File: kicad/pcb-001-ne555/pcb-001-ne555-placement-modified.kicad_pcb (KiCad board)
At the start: 2 copper layers, 14 parts, among them J1 +5 V / GND power input, U1 NE555D

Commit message: Update project files 2026-08-16 01:39:38
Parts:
- moved TP3 33.3 mm to (134.5, 108.0)
- moved RV1 24.8 mm to (107.0, 117.0), turned to -90 degrees
- moved D1 21.8 mm to (130.7, 117.4)
- moved U1 21.6 mm to (127.2, 107.6), turned to 180 degrees
- moved TP4 19.7 mm to (117.0, 110.5)
- moved R2 19.3 mm to (110.5, 100.2), turned to -90 degrees
- moved R1 18.9 mm to (106.5, 90.4), turned to -90 degrees
- moved C1 16.1 mm to (114.2, 104.0)
- moved R3 14.0 mm to (129.9, 101.9)
- moved C2 13.3 mm to (111.8, 95.8)
- moved J1 13.1 mm to (125.2, 88.2)
- moved TP1 4.48 mm to (106.5, 86.0)
- moved TP2 4.00 mm to (110.8, 86.0)
- moved C3 3.54 mm to (121.5, 112.8)
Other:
- board outline added: 39.2 x 41.8 mm

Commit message: Update project files 2026-08-16 14:48:06
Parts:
- U1: value NE555D -> NE555P
- moved TP2 38.6 mm to (139.8, 111.5)
- moved TP1 12.3 mm to (118.8, 85.8)
- moved J1 11.0 mm to (136.0, 86.2), turned to -90 degrees
- moved R1 5.02 mm to (106.0, 85.4)
- moved R2 4.49 mm to (110.5, 95.7)
- moved C2 4.26 mm to (112.0, 91.5)
- moved TP4 2.76 mm to (114.2, 110.2)
- moved RV1 2.37 mm to (109.2, 118.0)
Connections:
- D1 pad 1: /VOUT -> Net-(D1-K)
- R3 pad 1: /VOUT -> Net-(D1-K)
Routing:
- net +5V: track 0.00 -> 69.8 mm
- net /VCAP: track 0.00 -> 33.7 mm
- net Net-(U1-DISCH): track 0.00 -> 28.7 mm
- net /VOUT: track 0.00 -> 19.4 mm
- net Net-(D1-K): track 0.00 -> 15.8 mm
- net Net-(R2-Pad2): track 0.00 -> 12.7 mm
- net Net-(U1-CONT): track 0.00 -> 11.0 mm
- net GND: track 0.00 -> 5.44 mm
- added copper zone on B.Cu, net GND
- added copper zone on F.Cu, net GND
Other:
- board size 39.2 x 41.8 mm -> 38.5 x 40.8 mm

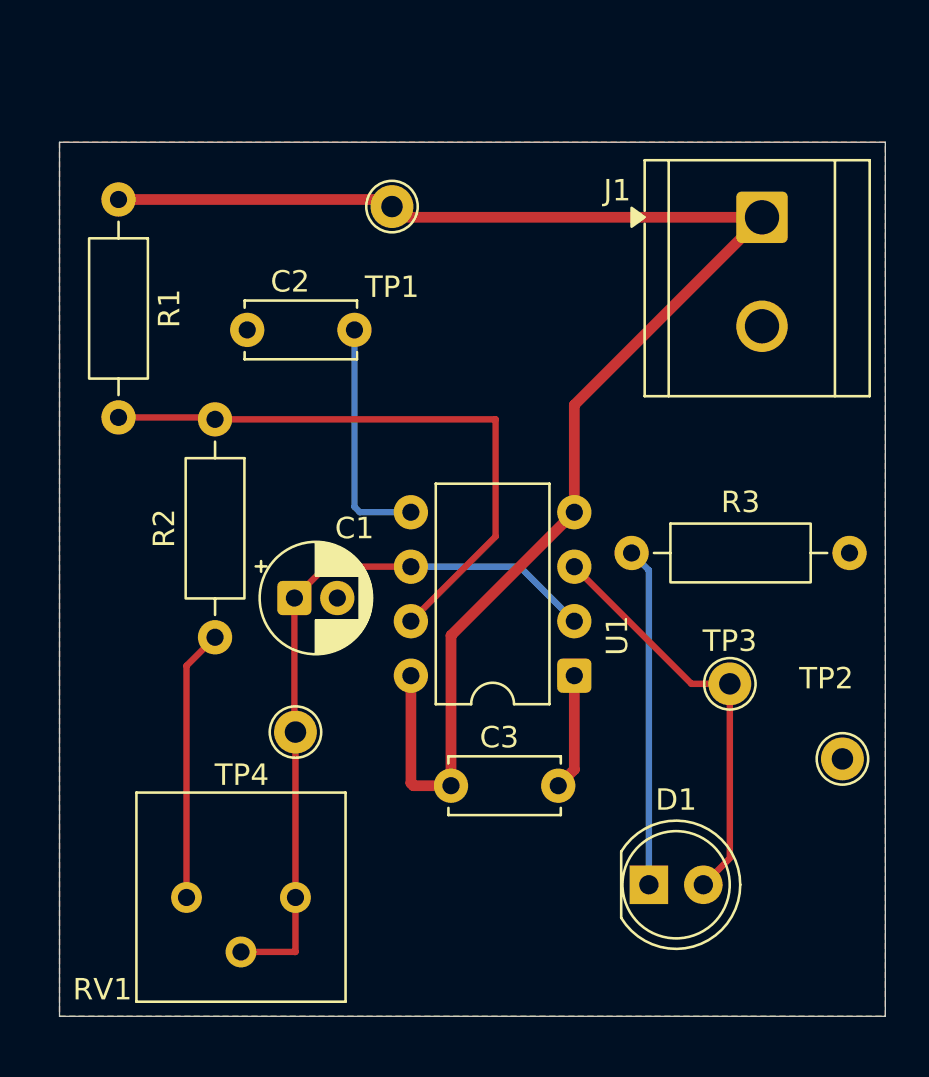
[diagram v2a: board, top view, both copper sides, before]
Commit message: docs: publish final PCB-001 engineering record
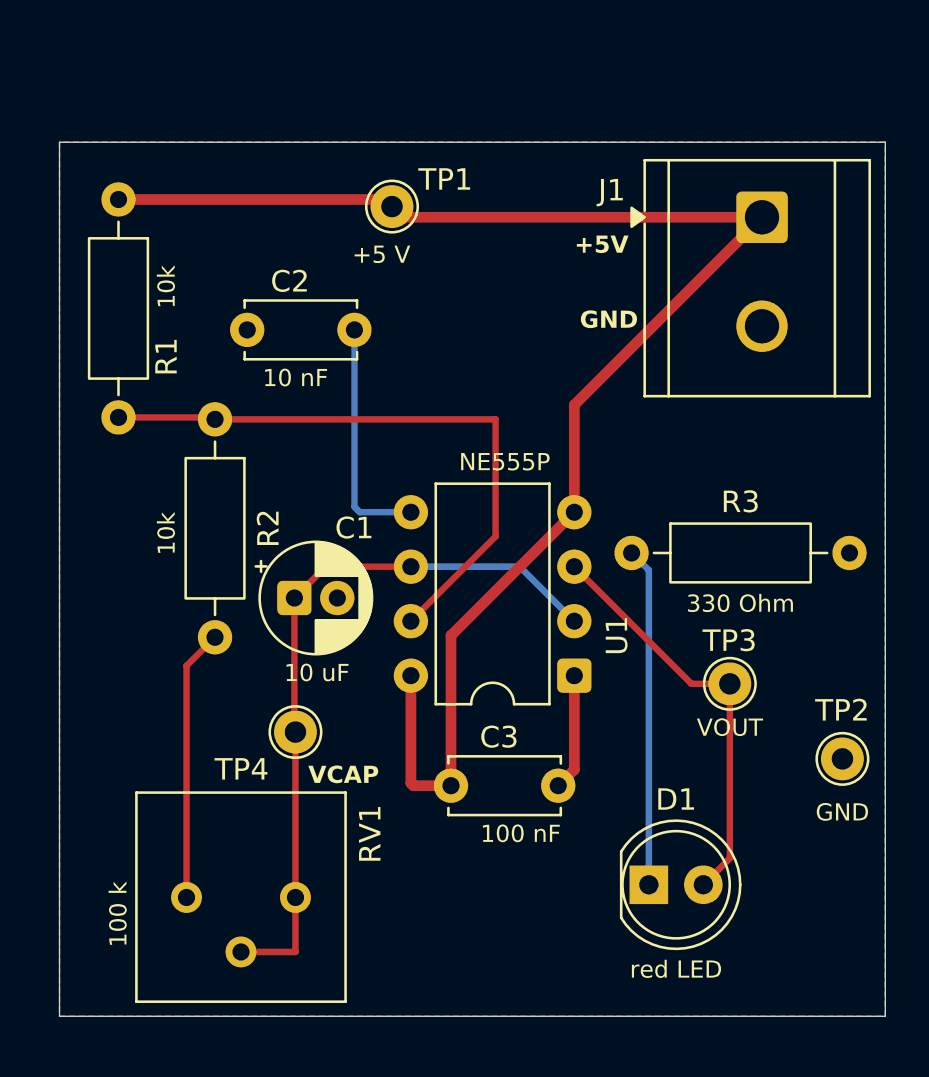
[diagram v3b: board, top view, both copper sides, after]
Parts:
- R1, R2: value 10 kOhm -> 10k
- RV1: value 100 kOhm -> 100 k
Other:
- board text added: "+5V"
- board text added: "GND"
